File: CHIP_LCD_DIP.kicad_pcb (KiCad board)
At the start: 2 copper layers, 42 x 61.5 mm, 25 parts, among them CON1 C.H.I.P., CON2 Power, IC1 74LVC138, IC2 DS2431, IC3 AP3032, IC4 74AHC1G08, P1 GPIO, P2 UART, P3 Pwr SW, P5 LCD

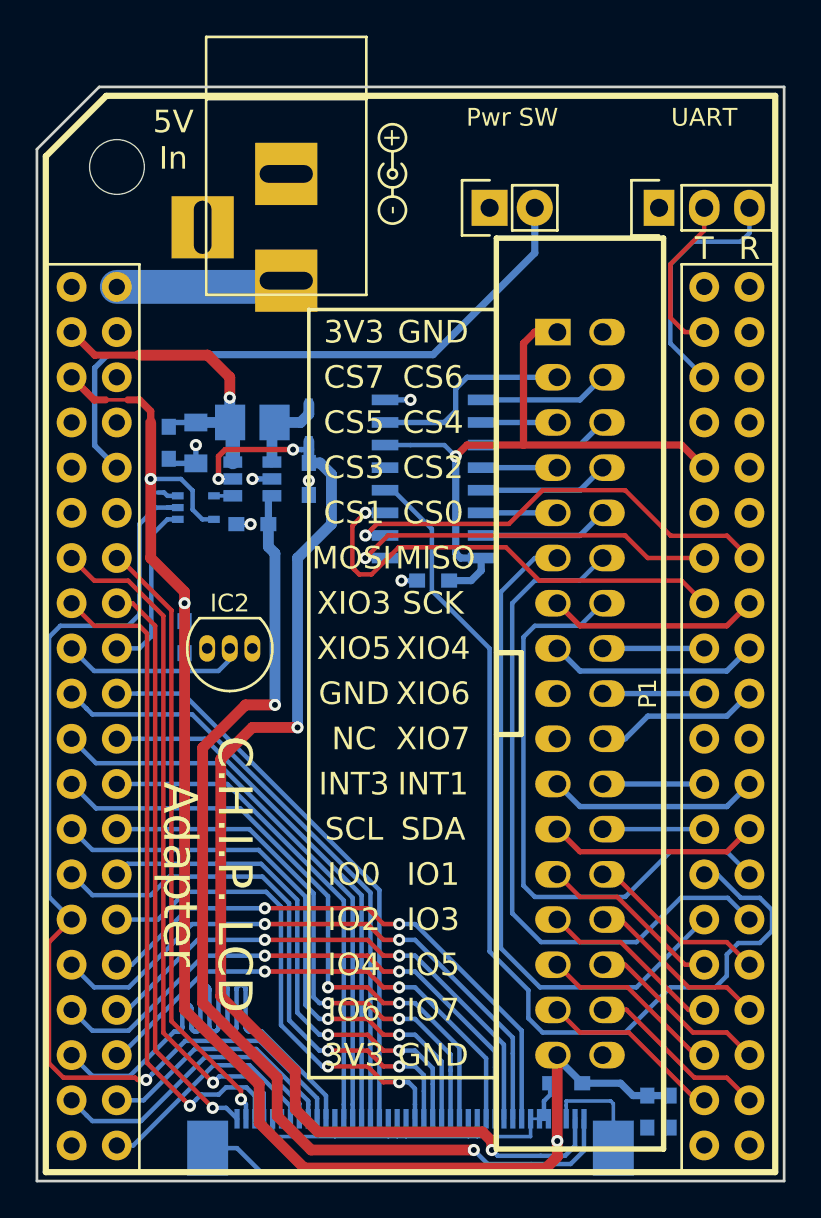
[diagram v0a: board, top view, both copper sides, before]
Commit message: Added connector to go to optional capacitive touch board.
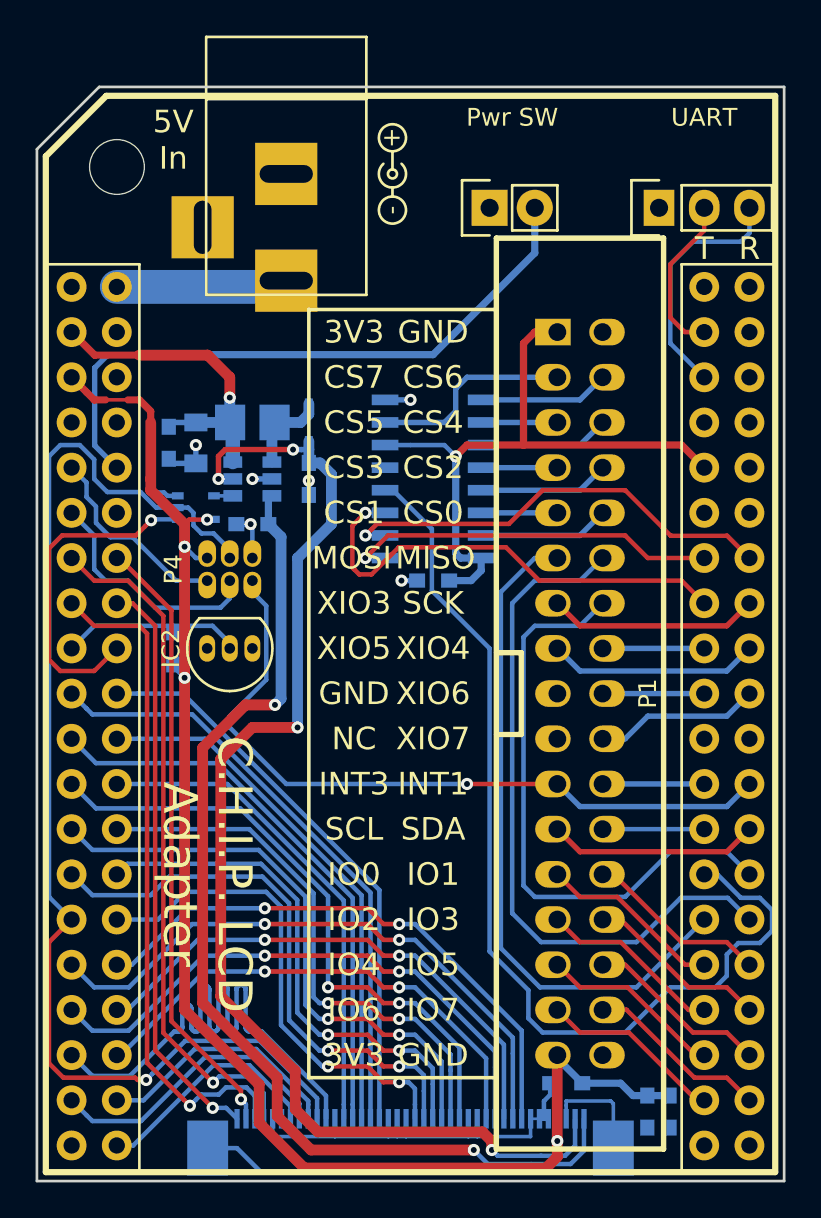
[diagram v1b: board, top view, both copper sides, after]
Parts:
- added P4: TS, connectors:02x03_Header_0.05, F.Cu at (83.8, 66.7)
- moved REF** 1.27 mm to (95.2, 73.7)
- moved R2 0.90 mm to (81.9, 71.1), turned to 90 degrees
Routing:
- net /INT3: track 11.8 -> 41.0 mm, vias 0 -> 1
- net /SCL1: track 0.00 -> 13.4 mm
- net /SDA1: track 0.00 -> 11.3 mm
- net /LCD_ON: track 57.7 -> 68.4 mm
- net /PWM: track 9.76 -> 18.8 mm, vias 0 -> 1
- net GND: track 64.9 -> 66.9 mm
- net /1W: track 11.3 -> 10.5 mm
- net +3V3: track 122.9 -> 122.3 mm, vias 4 -> 5

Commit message: Updated files. Added source code. Added pdf copies of design files.
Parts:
- P3: footprint Pin_Headers:Pin_Header_Straight_1x02 -> Pin_Headers:Pin_Header_Angled_1x02
- P4: renamed from P2; footprint Pin_Headers:Pin_Header_Straight_1x03 -> Pin_Headers:Pin_Header_Angled_1x03
- moved P1 1.27 mm to (77.5, 50.8)
- moved REF** 1.02 mm to (94.2, 43.4)
- renumbered CON1 to P1, CON2 to P2, P1 to P6, P4 to P7
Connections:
- P6 pad 13: /XIO3 -> GND
- P6 pad 15: /XIO5 -> /XIO3
- P6 pad 17: GND -> /XIO5
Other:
- board size 42 x 61.5 mm -> 41.4 x 61.1 mm
- board text removed: "R"
- board text removed: "T"
